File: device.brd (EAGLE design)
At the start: 76.2 x 76.2 mm, 40 parts, among them P1 ST9S008V4AR1500, P2 S2B-PH-SM4-TB(LF)(SN), Q1 FDN340P, U1 RPI_COMPUTE, U2 LMR10510YMFE/NOPB, U3 LMR10510YMFE/NOPB, U4 MCP73832T-2ACI/OT

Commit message: Modify board
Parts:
- moved R11 12.5 mm to (44.5, 41.9), turned to 0 degrees
- moved R12 10.9 mm to (49.5, 41.9), turned to 0 degrees
- moved R15 6.35 mm to (19.1, 45.7)
- moved R7 4.58 mm to (16.5, 41.9), turned to 90 degrees
- moved D3 3.81 mm to (49.5, 47.0)
- moved U4 2.84 mm to (48.3, 58.4)
- moved Q1 2.54 mm to (50.8, 53.3)
- moved P1 2.54 mm to (71.1, 48.3)
- moved P2 1.27 mm to (50.8, 66.0)
- moved R13 1.27 mm to (54.6, 59.7)
- moved R9 1.27 mm to (24.1, 41.9), turned to 90 degrees
- moved R8 1.27 mm to (20.3, 41.9), turned to 90 degrees
- moved R10 1.27 mm to (27.9, 41.9), turned to 90 degrees

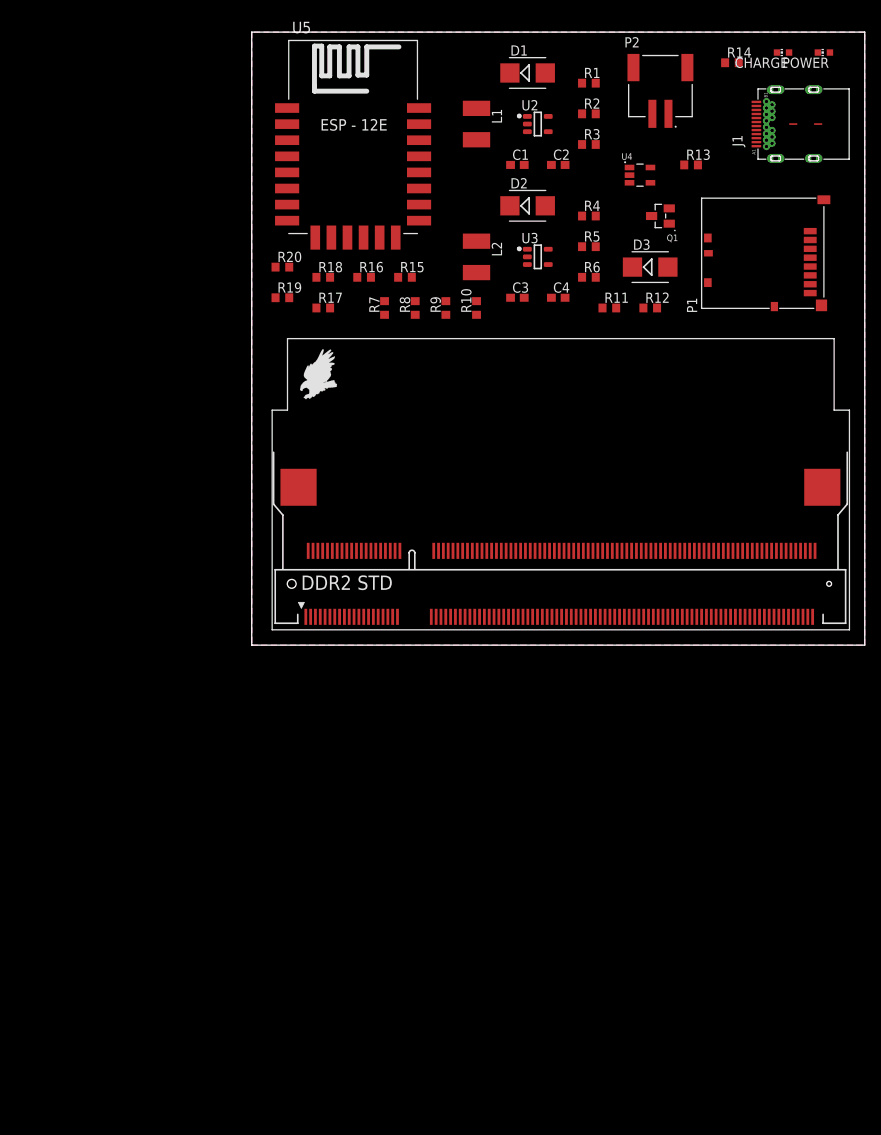
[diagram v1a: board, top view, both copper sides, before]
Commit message: Modify layout and add PAM2306
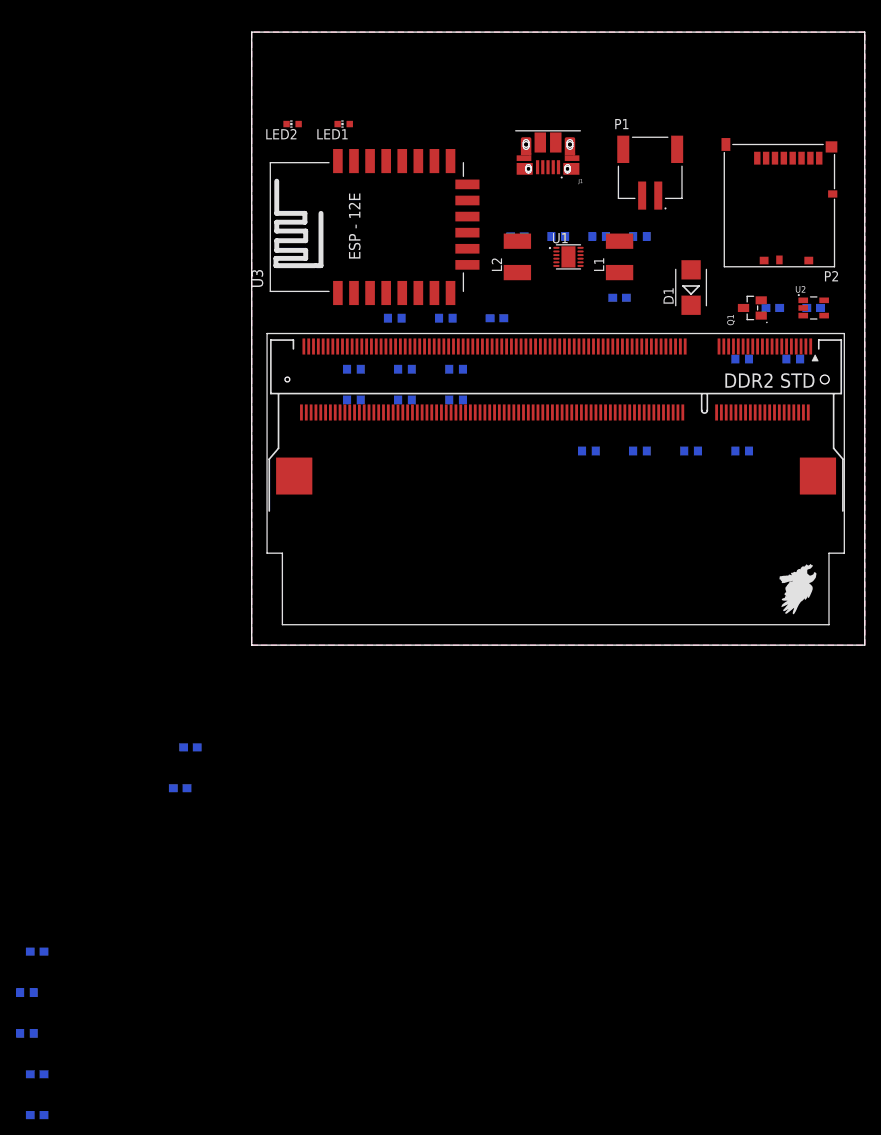
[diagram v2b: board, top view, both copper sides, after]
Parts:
- removed CHARGE, POWER: (no value), led:CHIP-LED0603
- removed D2, D3: (no value), diode:SMB
- removed R20: 33, resistor:R0603
- removed U4: MCP73832T-2ACI/OT, Common-Parts-Library-Eagle:SOT95P270X145-5N
- removed U5: (no value), esp8266modules:ESP12E-SMD
- added C10, C5, C6, C7, C9: 10uF, resistor:C0603
- added C8: 100nF, resistor:C0603
- added LED1, LED2: (no value), led:CHIP-LED0603
- added PCB1: RPI_COMPUTE, e14_Rpi_Compute_RevC:RPI_COMPUTE
- C1: value 22uF -> 10uF
- C2: value 22uF -> 1uF
- C3, C4: value 22uF -> 2.7uF
- J1: value (none) -> 10103594-0001LF; device Wurth_Elektronik_Electromechanic_Input-Output_Connectors_rev17b:632723X00011 -> Common-Parts-Library-Eagle:FCI_10103594-0001LF
- L1, L2: value 1.6uH -> 4.7uH
- P1: value ST9S008V4AR1500 -> S2B-PH-SM4-TB(LF)(SN); device Common-Parts-Library-Eagle:JAE_ST9S008V4AR1500 -> Common-Parts-Library-Eagle:JST_S2B-PH-SM4-TB(LF)(SN)
- P2: value S2B-PH-SM4-TB(LF)(SN) -> ST9S008V4AR1500; device Common-Parts-Library-Eagle:JST_S2B-PH-SM4-TB(LF)(SN) -> Common-Parts-Library-Eagle:JAE_ST9S008V4AR1500
- Q1: value FDN340P -> SSM3J328R,LF; device Common-Parts-Library-Eagle:FDN340P_SOT95P240X120-3N -> Common-Parts-Library-Eagle:SOT95P240X88-3N
- R1: value 45K -> 100K
- R11: value 470 -> 100K
- R12: value 2K -> 100K
- R14: value 470 -> 33
- R2: value 10K -> 470
- R3: value 100K -> 54K
- R4: value 20K -> 12K
- R5: value 10K -> 20K
- R7: value 100K -> 10K
- R8: value 100K -> 470
- R9: value 100K -> 2K
- U1: value RPI_COMPUTE -> PAM2306DYPAA; device e14_Rpi_Compute_RevC:RPI_COMPUTE -> PAM2306DYPAA:SON45P300X300X80-13N
- U2: value LMR10510YMFE/NOPB -> MCP73832T-2ACI/OT; device Common-Parts-Library-Eagle:LMR10510YMFE/NOPB_SOT95P280X145-5N -> Common-Parts-Library-Eagle:SOT95P270X145-5N
- U3: value LMR10510YMFE/NOPB -> (none); device Common-Parts-Library-Eagle:LMR10510YMFE/NOPB_SOT95P280X145-5N -> esp8266modules:ESP12E-SMD
- moved C1 132.3 mm to (-26.7, -58.4), flipped to the bottom
- moved R4 119.1 mm to (-27.9, -43.2), flipped to the bottom
- moved R7 100.5 mm to (-27.9, -48.3), flipped to the bottom, turned to 0 degrees
- moved R14 63.0 mm to (12.7, 30.5), flipped to the bottom
- moved R8 47.4 mm to (67.3, 35.6), flipped to the bottom, turned to 0 degrees
- moved U2 41.2 mm to (69.8, 41.9)
- moved U1 40.7 mm to (39.4, 48.3)
- moved R13 37.8 mm to (41.9, 24.1), flipped to the bottom
- moved R10 37.5 mm to (61.0, 24.1), flipped to the bottom, turned to 0 degrees
- moved R9 37.4 mm to (61.0, 35.6), flipped to the bottom, turned to 0 degrees
- moved C3 36.9 mm to (69.8, 41.9), flipped to the bottom
- moved R2 35.0 mm to (17.8, 40.6), flipped to the bottom
- moved R1 34.2 mm to (24.1, 40.6), flipped to the bottom
- moved D1 33.5 mm to (54.6, 44.5), turned to 90 degrees
- moved C2 32.1 mm to (64.8, 41.9), flipped to the bottom
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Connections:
- removed net N$13: R4.2, R5.2, U3.3
- new net USB_OTGID: PCB1.168
- net +CM_1V8: now also C6.2, C7.2, PCB1.183, PCB1.184, PCB1.185, PCB1.186, R5.2; no longer C4.2, R4.1, U1.183, U1.184, U1.185, U1.186
- net +CM_3V3: now also C1.2, C5.2, P2.4, PCB1.189, PCB1.190, PCB1.191, PCB1.192, PCB1.193, PCB1.194, PCB1.197, PCB1.198, PCB1.199, PCB1.200, PCB1.39, PCB1.4, PCB1.40, PCB1.41, PCB1.42, PCB1.6, R2.2, R3.2, U3.VCC; no longer C2.2, P1.4, R1.1, R14.2, R6.2, U1.189, U1.190, U1.191, U1.192, U1.193, U1.194, U1.197, U1.198, U1.199, U1.200, U1.39, U1.4, U1.40, U1.41, U1.42, U1.6, U5.VCC
- net +VBAT: now also C3.2, P1.1, U2.3; no longer P2.1, U4.3
- net +VSUP: now also C4.2, D1.A, J1.1, R1.2, R8.2, U2.4; no longer D3.A, J1.A4, J1.A9, J1.B4, J1.B9, R11.2, R13.2, U4.4
- net +VSYS: now also C10.2, C2.2, C9.2, D1.C, R6.2, U1.1, U1.6, U1.7; no longer C1.2, C3.2, D3.C, R3.2, U2.5, U3.5
- net GND: now also C10.1, C6.1, C8.1, C9.1, J1.5, LED1.C, P1.2, P2.6, PCB1.1, PCB1.103, PCB1.104, PCB1.109, PCB1.110, PCB1.115, PCB1.116, PCB1.121, PCB1.13, PCB1.133, PCB1.134, PCB1.139, PCB1.14, PCB1.140, PCB1.145, PCB1.146, PCB1.151, PCB1.152, PCB1.163, PCB1.164, PCB1.169, PCB1.170, PCB1.181, PCB1.182, PCB1.187, PCB1.188, PCB1.19, PCB1.195, PCB1.196, PCB1.20, PCB1.25, PCB1.26, PCB1.31, PCB1.32, PCB1.37, PCB1.38, PCB1.43, PCB1.44, PCB1.49, PCB1.50, PCB1.55, PCB1.56, PCB1.61, PCB1.62, PCB1.67, PCB1.68, PCB1.7, PCB1.73, PCB1.74, PCB1.79, PCB1.8, PCB1.80, PCB1.85, PCB1.86, PCB1.91, PCB1.92, PCB1.97, PCB1.98, R1.1, R11.1, R4.1, U1.3, U1.9, U3.GND; no longer D1.A, D2.A, J1.A1, J1.A12, J1.B1, J1.B12, P1.6, P2.2, POWER.C, R2.1, R5.1, R8.1, U1.1, U1.103, U1.104, U1.109, U1.110, U1.115, U1.116, U1.121, U1.133, U1.134, U1.139, U1.14, U1.140, U1.145, U1.146, U1.151, U1.152, U1.163, U1.164, U1.169, U1.170, U1.181, U1.182, U1.187, U1.188, U1.19, U1.195, U1.196, U1.20, U1.25, U1.26, U1.31, U1.32, U1.37, U1.38, U1.43, U1.44, U1.49, U1.50, U1.55, U1.56, U1.61, U1.62, U1.67, U1.68, U1.7, U1.73, U1.74, U1.79, U1.8, U1.80, U1.85, U1.86, U1.91, U1.92, U1.97, U1.98, U3.2, U4.2, U5.GND
- net N$1: now also PCB1.84, R13.2; no longer R10.2, U1.84
- net N$10: now also C7.1, R5.1, R7.2, U1.10; no longer R1.2, R2.2, U2.3
- net N$11: now also L1.1, U1.8; no longer D2.C, L2.1, U3.1
- net N$12: now also L2.1, U1.2; no longer D1.C, L1.1, U2.1
- net N$14: now also LED1.A, R2.1; no longer POWER.A, R14.1
- net N$15: now also R19.2, U3.SCLK; no longer R15.2, U5.SCLK
- net N$16: now also R18.2, U3.MOSI; no longer R16.2, U5.MOSI
- net N$17: now also U3.GPIO10; no longer U5.GPIO10
- net N$18: now also R16.2, U3.GPIO9; no longer R18.2, U5.GPIO9
- net N$19: now also R15.2, U3.MISO; no longer R19.2, U5.MISO
- net N$2: now also C8.2, U1.12; no longer U3.4
- net N$20: now also R14.2, U3.CS0; no longer R20.2, U5.CS0
- net N$3: now also LED2.C, U2.1; no longer CHARGE.C, U4.1
- net N$4: now also R9.2, U2.5; no longer R12.2, U4.5
- net N$5: now also LED2.A, R8.1; no longer CHARGE.A, R11.1
- net N$6: now also PCB1.28, R10.2; no longer R7.2, U1.28
- net N$7: now also PCB1.30, R11.2; no longer R8.2, U1.30
- net N$8: now also C5.1, R4.2, U1.4; no longer U2.4
- net N$9: now also PCB1.82, R12.2; no longer R9.2, U1.82
- net SDIO_CLK: now also PCB1.75, R19.1; no longer R15.1, U1.75
- net SDIO_CMD: now also PCB1.77, R14.1; no longer R20.1, U1.77
- net SDIO_D0: now also PCB1.81, R15.1; no longer R19.1, U1.81
- net SDIO_D1: now also PCB1.83, R18.1; no longer R16.1, U1.83
- net SDIO_D2: now also PCB1.87, R16.1; no longer R18.1, U1.87
- net SDIO_D3: now also PCB1.89; no longer U1.89
- net SDIO_ID: now also PCB1.3, U3.CH_PD; no longer U1.3, U5.CH_PD
- net SDX_CLK: now also P2.5, PCB1.10; no longer P1.5, U1.10
- net SDX_CMD: now also P2.3, PCB1.12; no longer P1.3, U1.12
- net SDX_D0: now also P2.7, PCB1.16; no longer P1.7, U1.16
- net SDX_D1: now also P2.8, PCB1.18; no longer P1.8, U1.18
- net SDX_D2: now also P2.1, PCB1.22; no longer P1.1, U1.22
- net SDX_D3: now also P2.2, PCB1.24; no longer P1.2, U1.24
- net USB_N: now also PCB1.167; no longer U1.167
- net USB_P: now also PCB1.165; no longer U1.165
